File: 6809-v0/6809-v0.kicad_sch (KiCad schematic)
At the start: 2 parts, among them U1 MC68B09

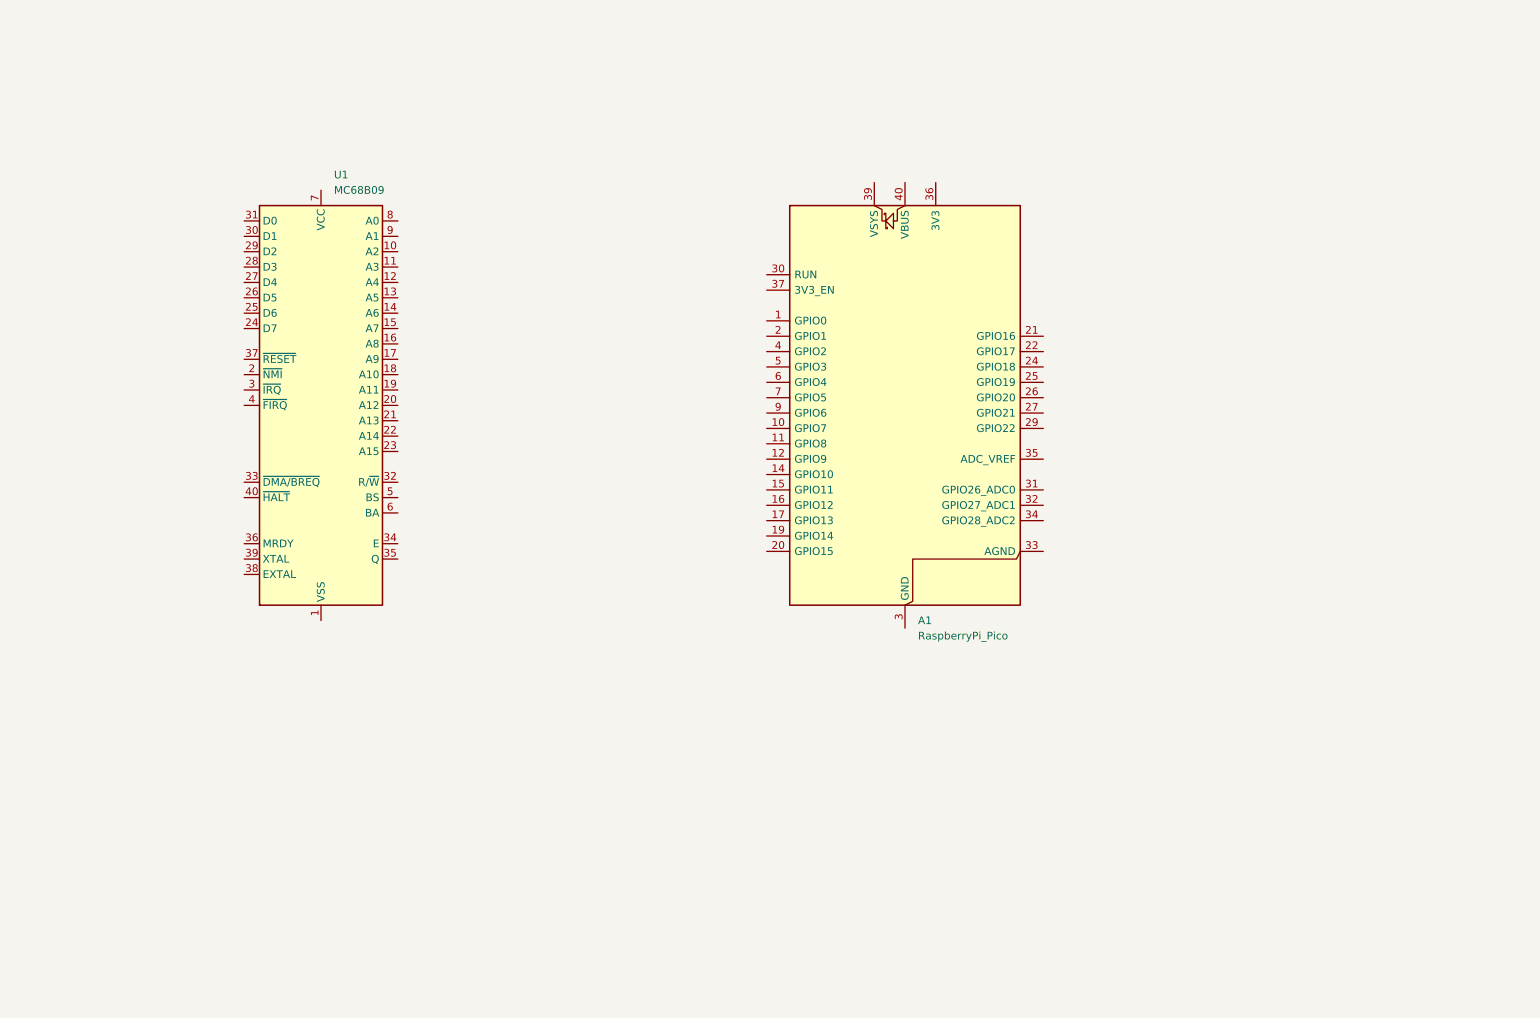
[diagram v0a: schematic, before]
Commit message: Added 6522 and 6551 symbols, plus SRAM and EPROM
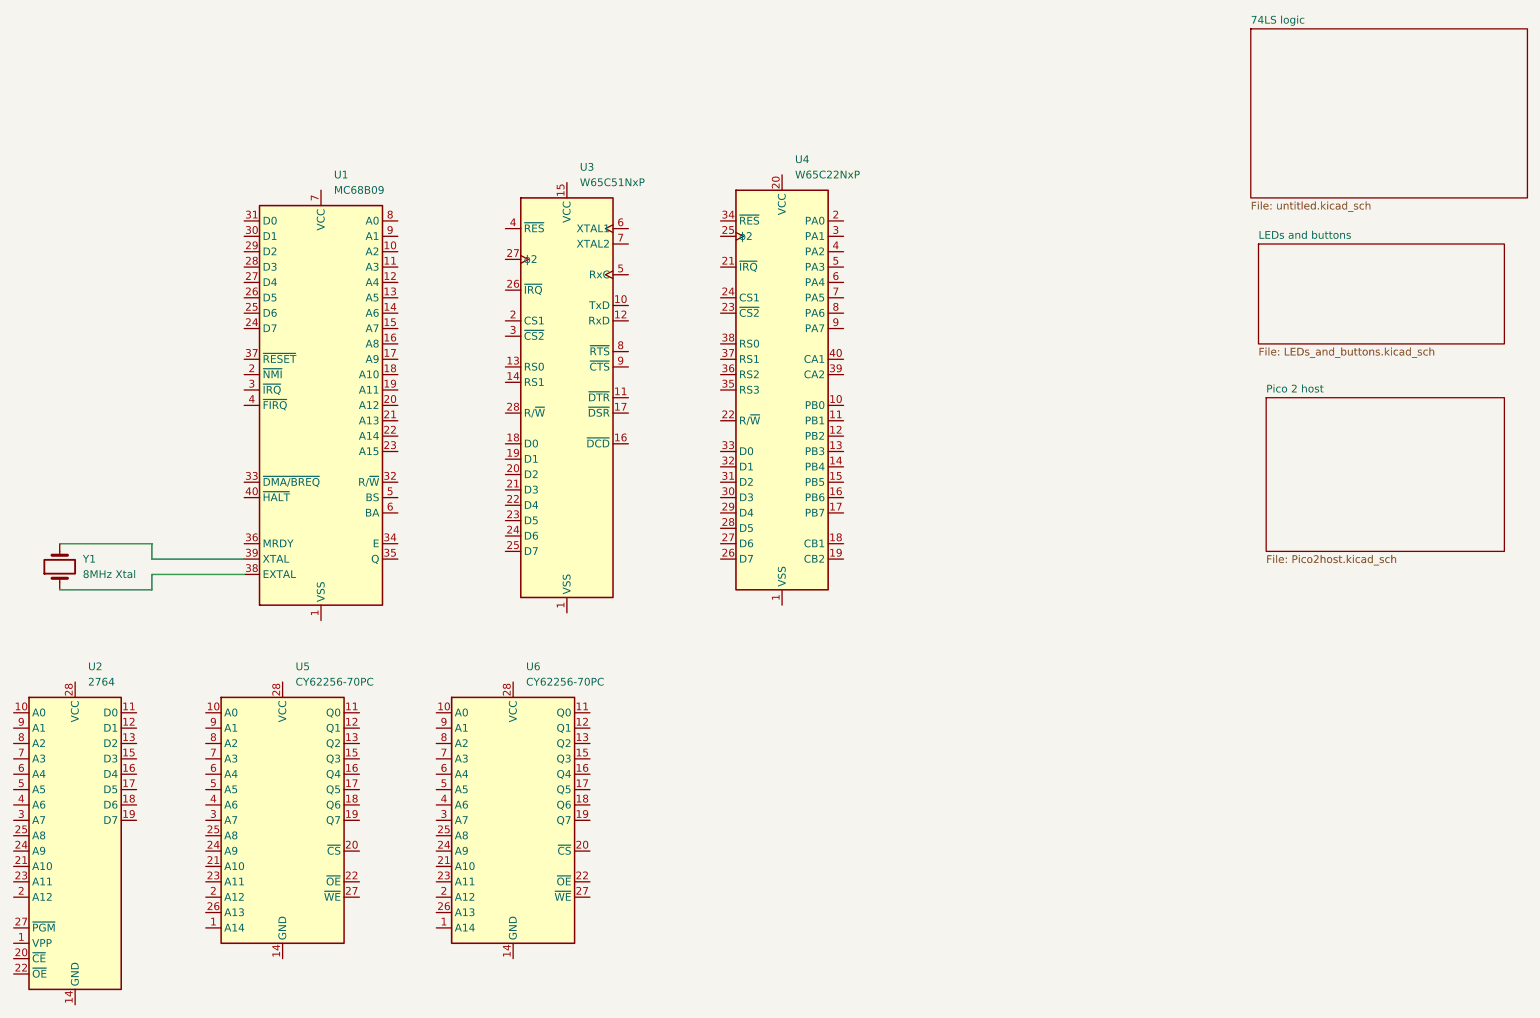
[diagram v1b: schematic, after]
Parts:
- removed A1: RaspberryPi_Pico, Module:RaspberryPi_Pico_Common_Unspecified, symbol MCU_Module:RaspberryPi_Pico
- added U2: 2764, Package_DIP:DIP-28_W15.24mm, symbol Memory_EPROM:2764
- added U3: W65C51NxP, Package_DIP:DIP-28_W15.24mm, symbol PCM_65xx-library:W65C51NxP
- added U4: W65C22NxP, Package_DIP:DIP-40_W15.24mm, symbol PCM_65xx-library:W65C22NxP
- added U5, U6: CY62256-70PC, Package_DIP:DIP-28_W15.24mm, symbol Memory_RAM:CY62256-70PC
- added Y1: 8MHz Xtal, symbol Device:Crystal
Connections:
- net at U1.38 (EXTAL): now also Y1.1
- net at U1.39 (XTAL): now also Y1.2
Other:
- added sheet 74LS logic (untitled.kicad_sch)
- added sheet LEDs and buttons (LEDs_and_buttons.kicad_sch)
- added sheet Pico 2 host (Pico2host.kicad_sch)
